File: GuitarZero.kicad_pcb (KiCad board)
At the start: 6 copper layers, 144 parts, among them J1 USB_A, J2 USB_B_Micro, J3 AudioJack3_SwitchT, J4 MCU_Debug, J6 Micro_SD_Card_Det_Hirose_DM3AT, SW1 SW_Push, SW2 SW_Push, SW3 SW_Push, SW4 SW_Push, SW5 SW_Push, SW6 SW_Push, U1 TPS54325, U10 FPGA_GPIO_Extra, U11 5x7 LED_matrix, U12 MCU_GPIO_Extra, U13 5x7 LED_matrix, U14 Power_Jumpers, U2 TSP54294, U3 XC7A100T-FTG256, U4 EFM32GG332, U5 S25FL127S, U6 Oscillator, U7 FPGA_JTAG_Debug, U8 PCM1754, U9 TPD_Current_Switch, Y1 Crystal_GND23

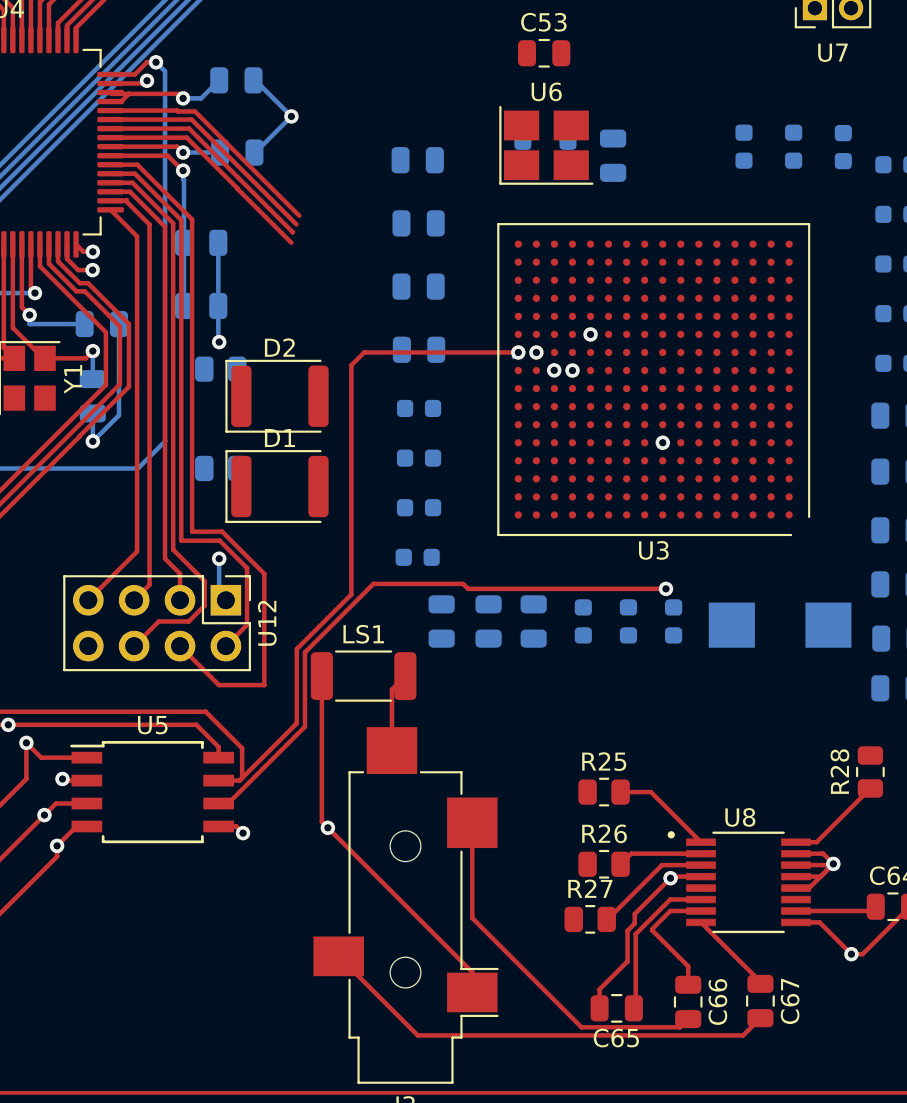
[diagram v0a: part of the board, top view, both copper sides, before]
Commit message: PCB: Grounded FPGA, wired MCU <-> FPGA
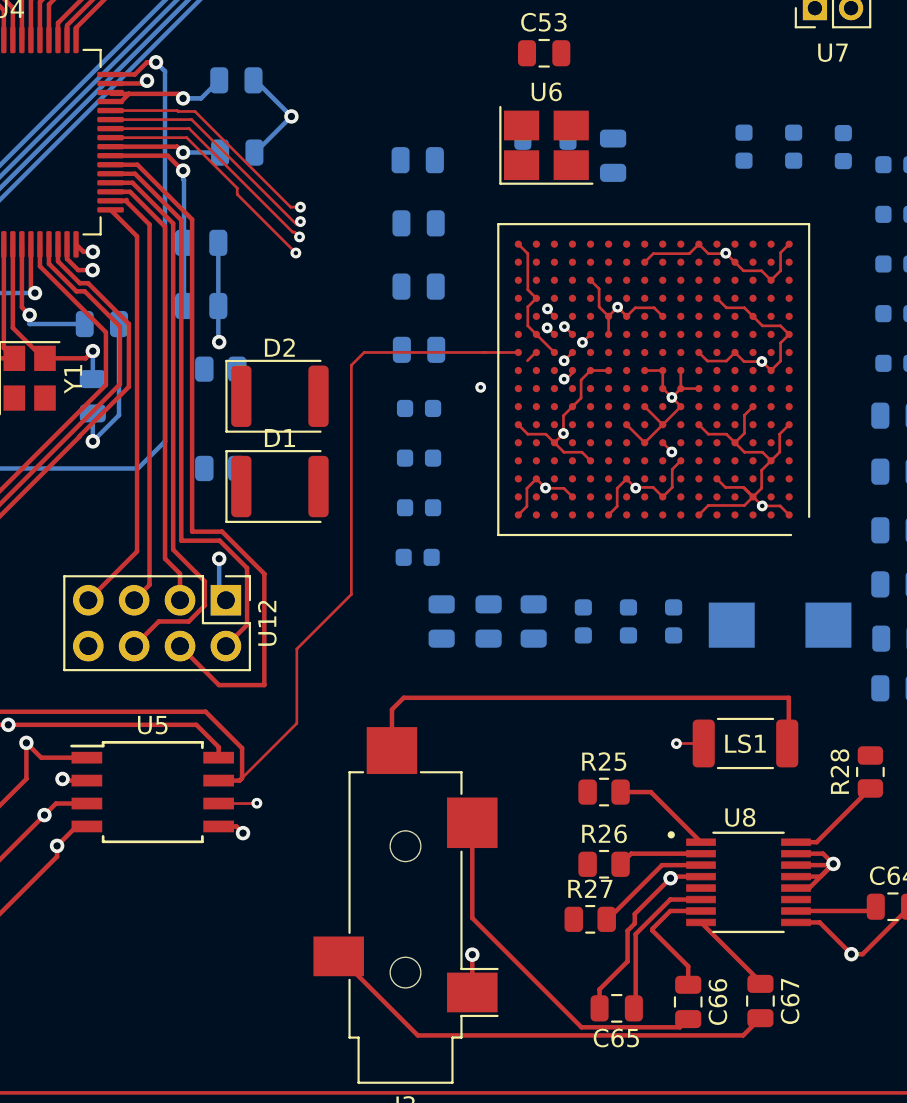
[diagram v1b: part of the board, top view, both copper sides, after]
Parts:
- moved LS1 21.5 mm to (202.8, 123.3)
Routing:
- net GND: track 327.6 -> 403.0 mm, vias 54 -> 63
- net Net-(J3-PadTN): track 4.43 -> 27.1 mm
- net /FPGA/MCU_SPI_MISO: track 12.9 -> 31.5 mm, vias 0 -> 2
- net /FPGA/MCU_SPI_Select: track 12.4 -> 31.0 mm, vias 0 -> 2
- net /FPGA/MCU_SPI_CLCK: track 12.5 -> 29.7 mm, vias 0 -> 2
- net /FPGA/MCU_SPI_MOSI: track 12.7 -> 29.5 mm, vias 0 -> 2
- net Net-(U3C-CCLK_0): track 41.4 -> 40.0 mm
- net Net-(U3A-IO_L2N_T0_D03_14): track 56.6 -> 56.3 mm, vias 1 -> 0
- net Net-(U3A-IO_L2P_T0_D02_14): track 53.4 -> 53.2 mm, vias 2 -> 1

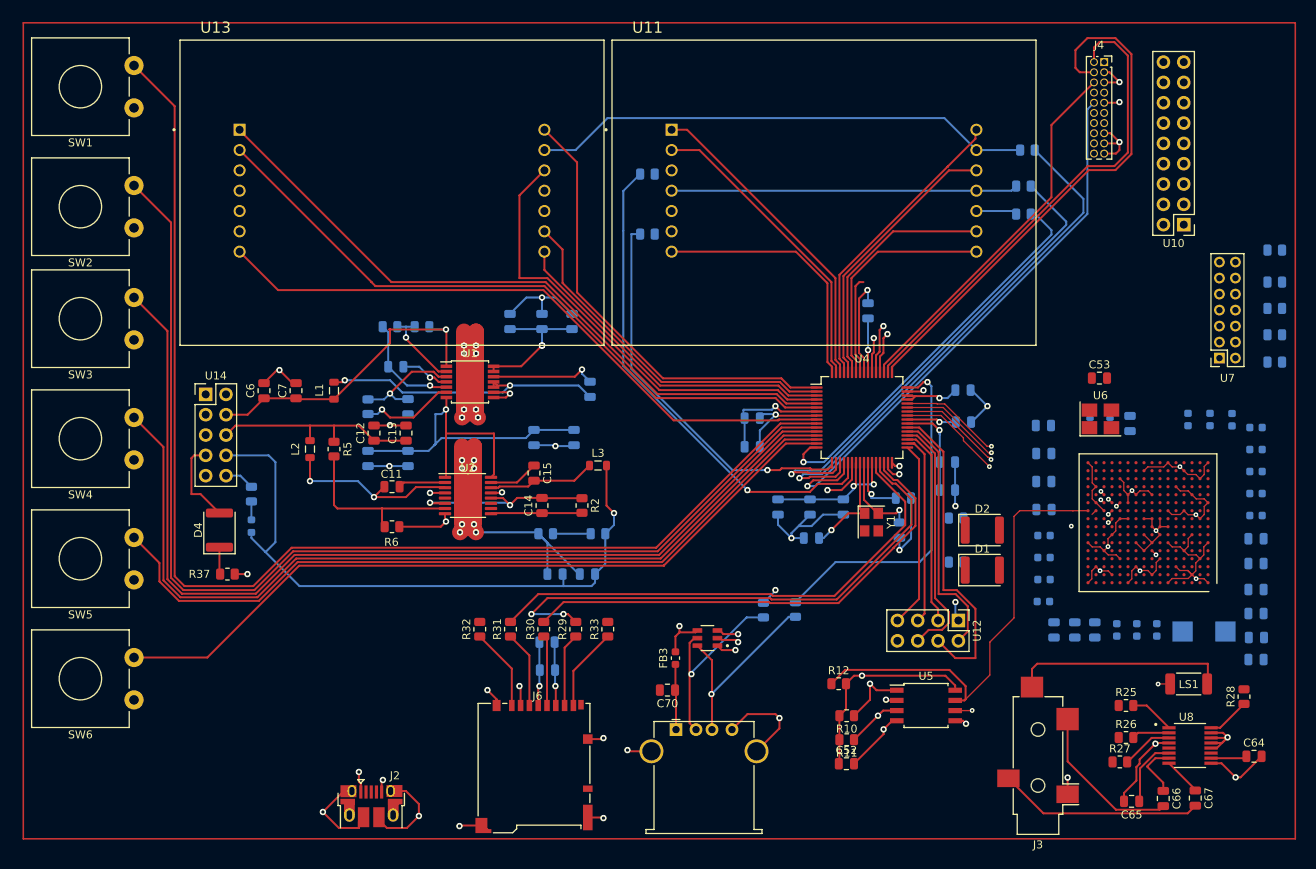
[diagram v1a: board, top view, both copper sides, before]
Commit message: Finished wiring for most of the FPGA
GPIO-extra pins remaining
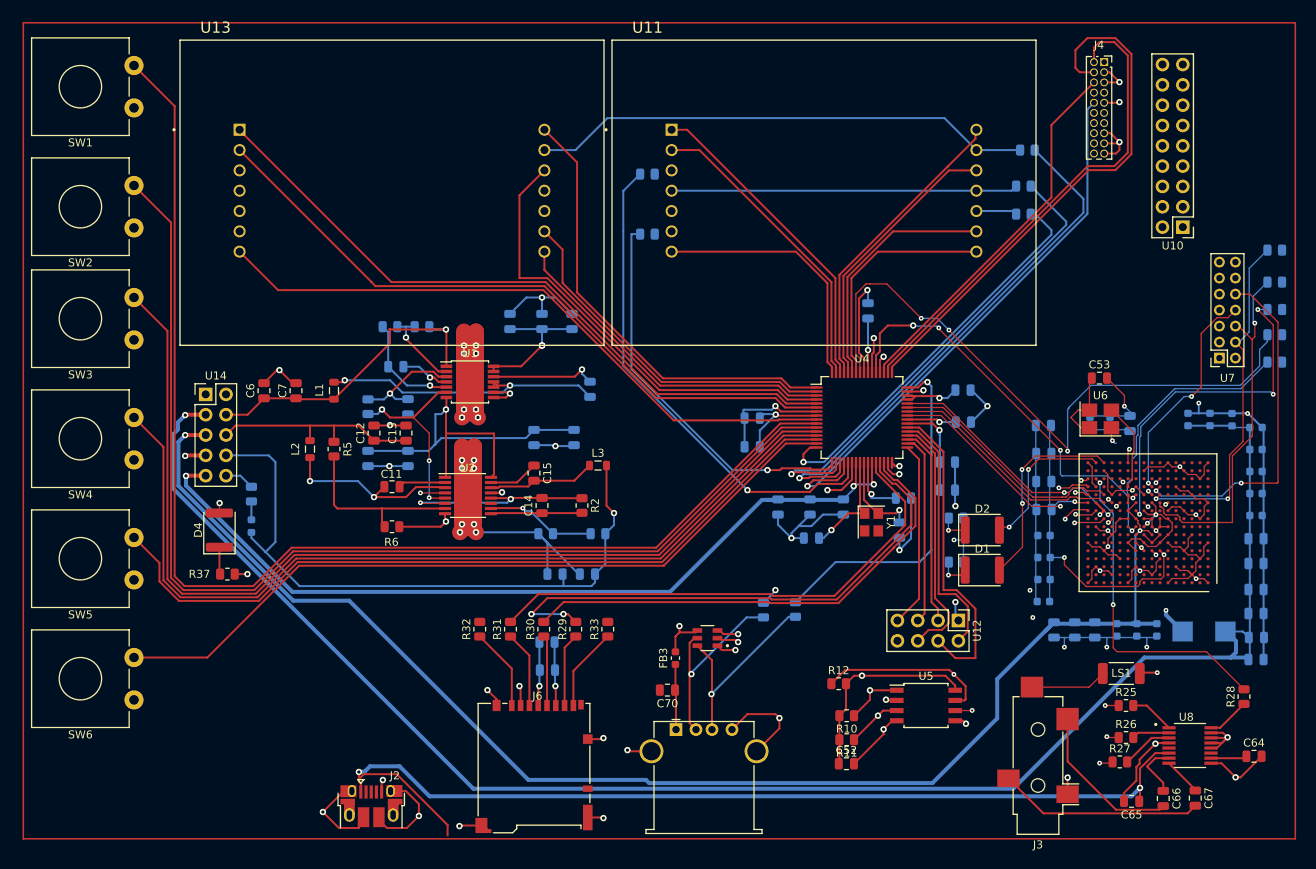
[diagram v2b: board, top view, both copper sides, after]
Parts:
- moved LS1 8.52 mm to (194.4, 122.0), turned to 180 degrees
- moved U10 0.33 mm to (202.1, 66.2)
- moved R15 0.14 mm to (213.6, 76.5)
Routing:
- net +1V0: track 0.00 -> 236.7 mm, vias 0 -> 3
- net +1V8: track 0.00 -> 192.1 mm, vias 0 -> 2
- net GND: track 403.0 -> 503.3 mm, vias 63 -> 77
- net +3.3VA: track 18.8 -> 116.3 mm, vias 2 -> 3
- net +5V: track 210.3 -> 304.1 mm, vias 5 -> 6
- net /FPGA/program_b: track 12.2 -> 95.8 mm, vias 0 -> 4
- net /FPGA/Done: track 6.15 -> 81.3 mm, vias 1 -> 4
- net +3.3V: track 93.5 -> 157.0 mm, vias 7 -> 16
- net Net-(U3C-TCK_0): track 0.00 -> 45.6 mm, vias 0 -> 1
- net /DAC/LEFT_RIGHT_CLOCK: track 0.00 -> 44.3 mm, vias 0 -> 2
- net Net-(U3C-TMS_0): track 0.00 -> 43.9 mm, vias 0 -> 2
- net Net-(U3C-TDI_0): track 0.00 -> 43.7 mm, vias 0 -> 2
- net Net-(U3C-INIT_B_0): track 0.00 -> 42.8 mm, vias 0 -> 3
- net /DAC/SYSTEM_CLOCK_INPUT: track 0.00 -> 40.5 mm, vias 0 -> 2
- net /DAC/DATA_INN: track 0.00 -> 40.4 mm, vias 0 -> 2
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
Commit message: Fixed 112 design error
FPGA GPIO pin headers still unrouted
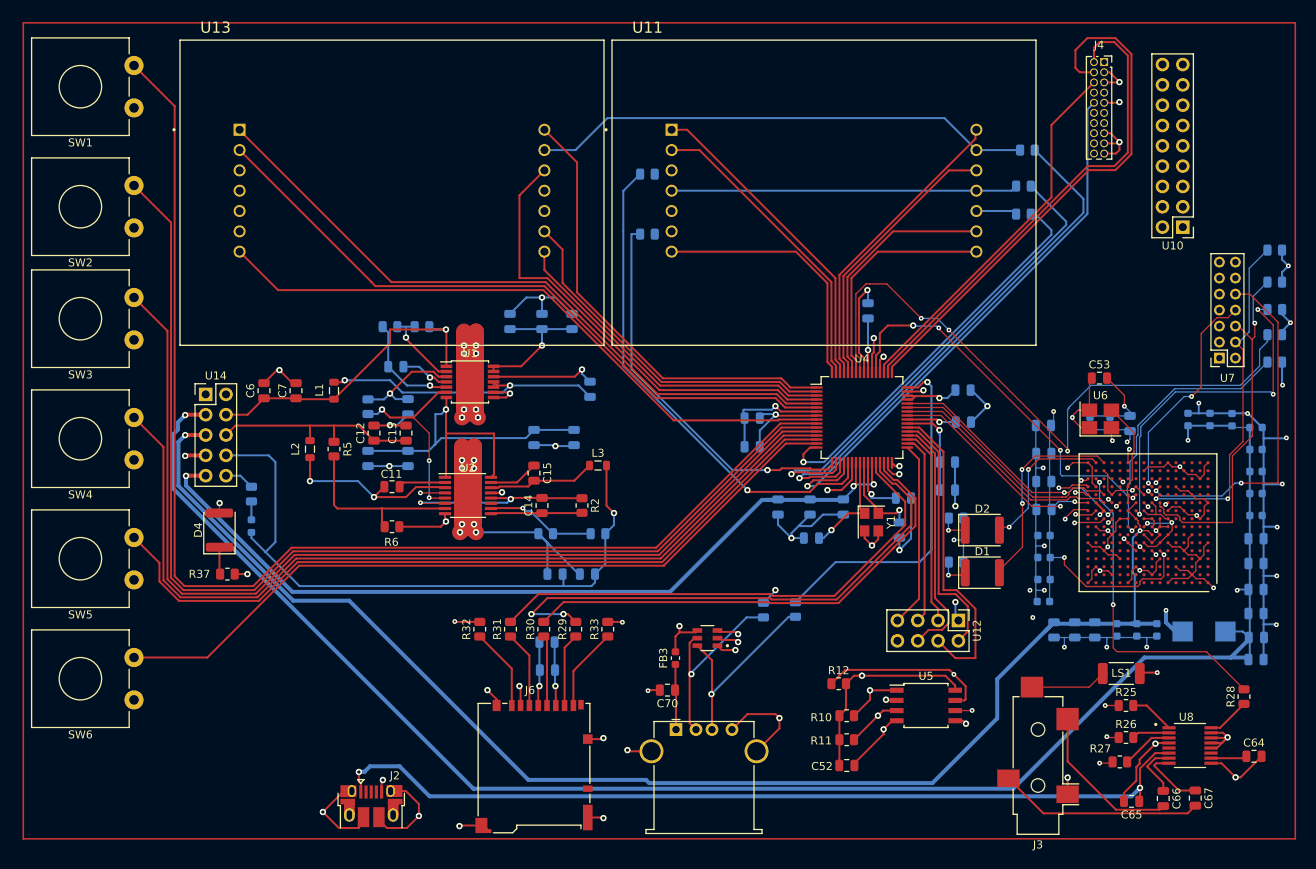
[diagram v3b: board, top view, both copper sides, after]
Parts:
- moved D1 0.33 mm to (177.0, 109.4)
- moved C52 0.23 mm to (160.1, 133.5)
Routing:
- net +1V0: track 236.7 -> 275.3 mm, vias 3 -> 7
- net GND: track 503.3 -> 529.2 mm, vias 77 -> 88
- net +3.3V: track 157.0 -> 174.2 mm, vias 16 -> 23
- net +5V: track 304.1 -> 289.5 mm, vias 6 -> 5
- net Net-(U8-VoutR): track 4.77 -> 8.44 mm
- net Net-(J6-DAT3/CD): track 66.2 -> 63.4 mm

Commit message: Moved board cutout to correct layer
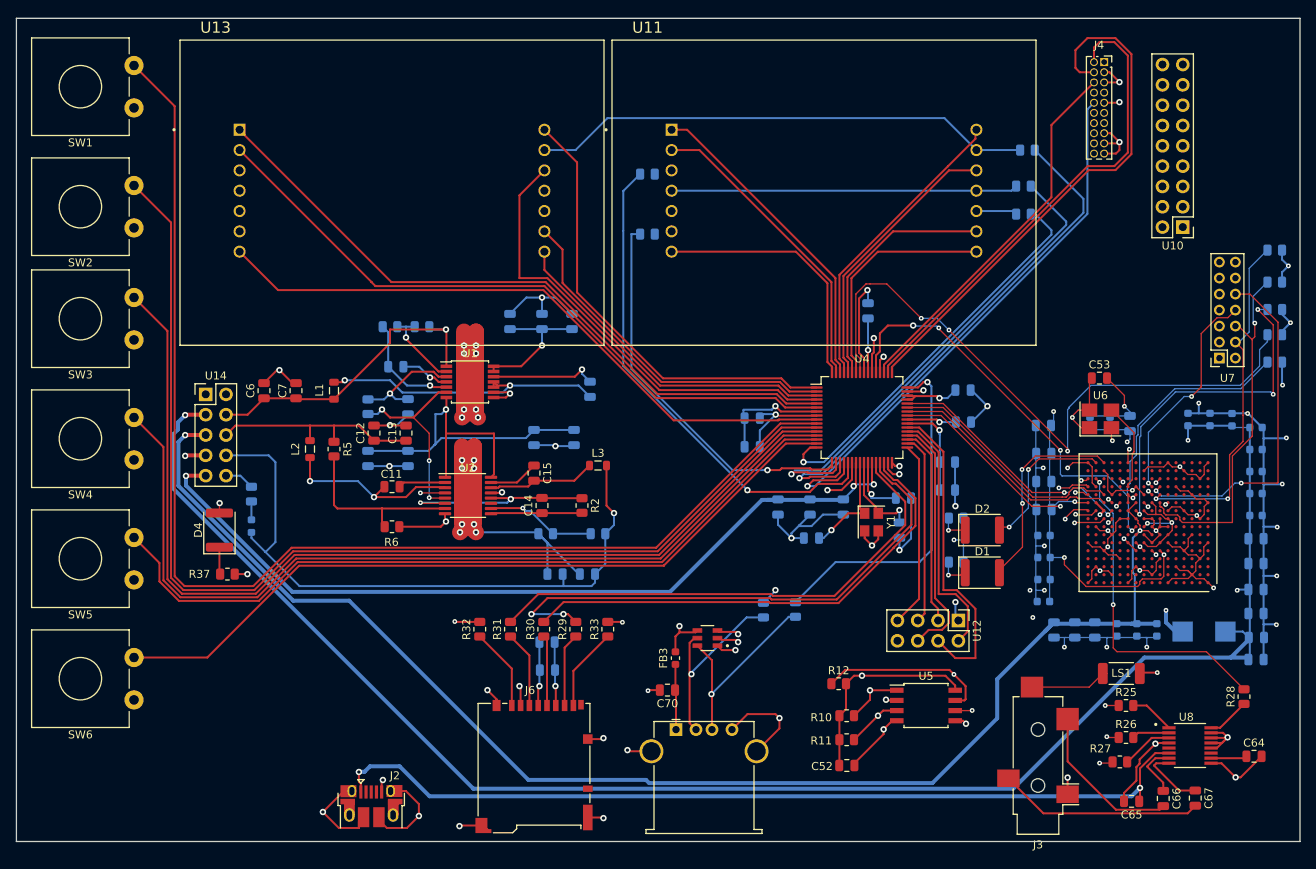
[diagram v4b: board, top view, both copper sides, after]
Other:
- board outline added: 160.4 x 102.9 mm
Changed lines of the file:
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@@
     )
   )
-  (gr_rect (start 57.161134 40.662942) (end 216.161134 142.662942)
-    (stroke (width 0.2) (type default)) (fill none) (layer "F.Cu"))
+  (gr_rect (start 56.3 40.1) (end 216.75 143)
+    (stroke (width 0.1) (type default)) (fill none) (layer "Edge.Cuts"))
   (segment (start 110.05 87.5) (end 110.05 88.95) (width 0.25) (layer "F.Cu") (net 1))
   (segment (start 196.75 136.3) (end 196.75 137.88) (width 0.25) (layer "F.Cu") (net 1))

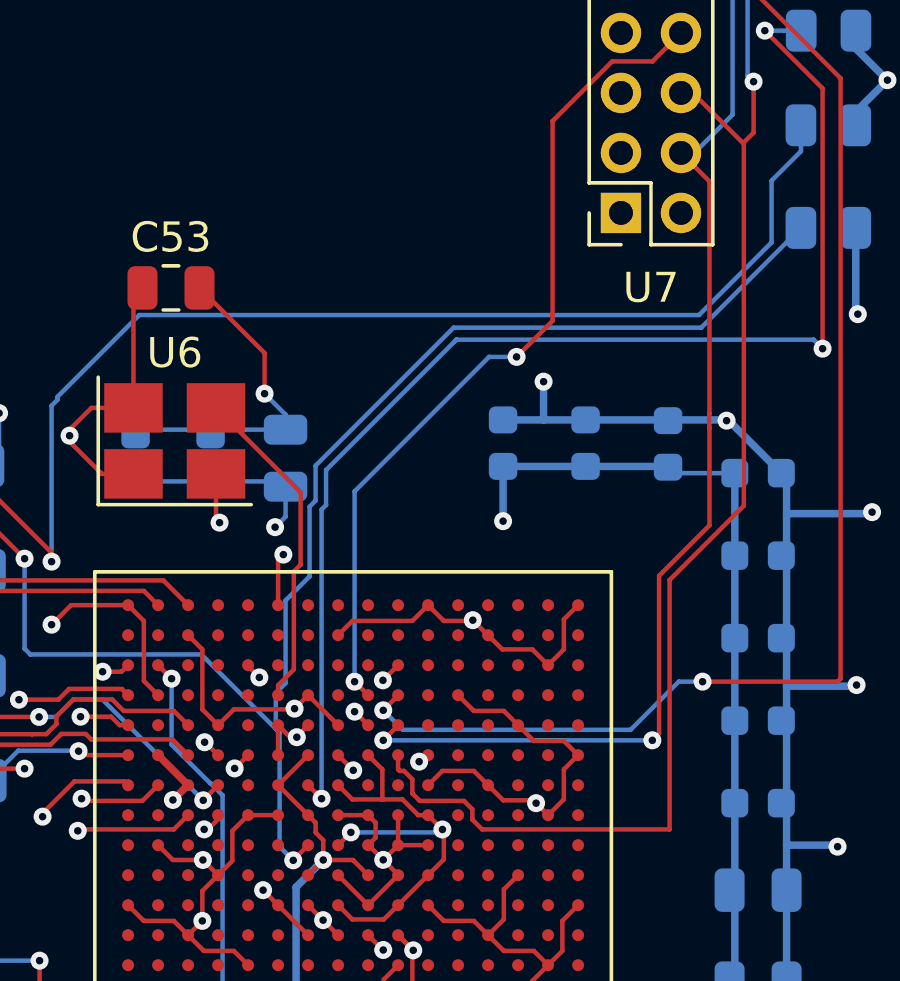
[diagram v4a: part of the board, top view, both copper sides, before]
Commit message: Grouped wires out from fpga to fpga pin header
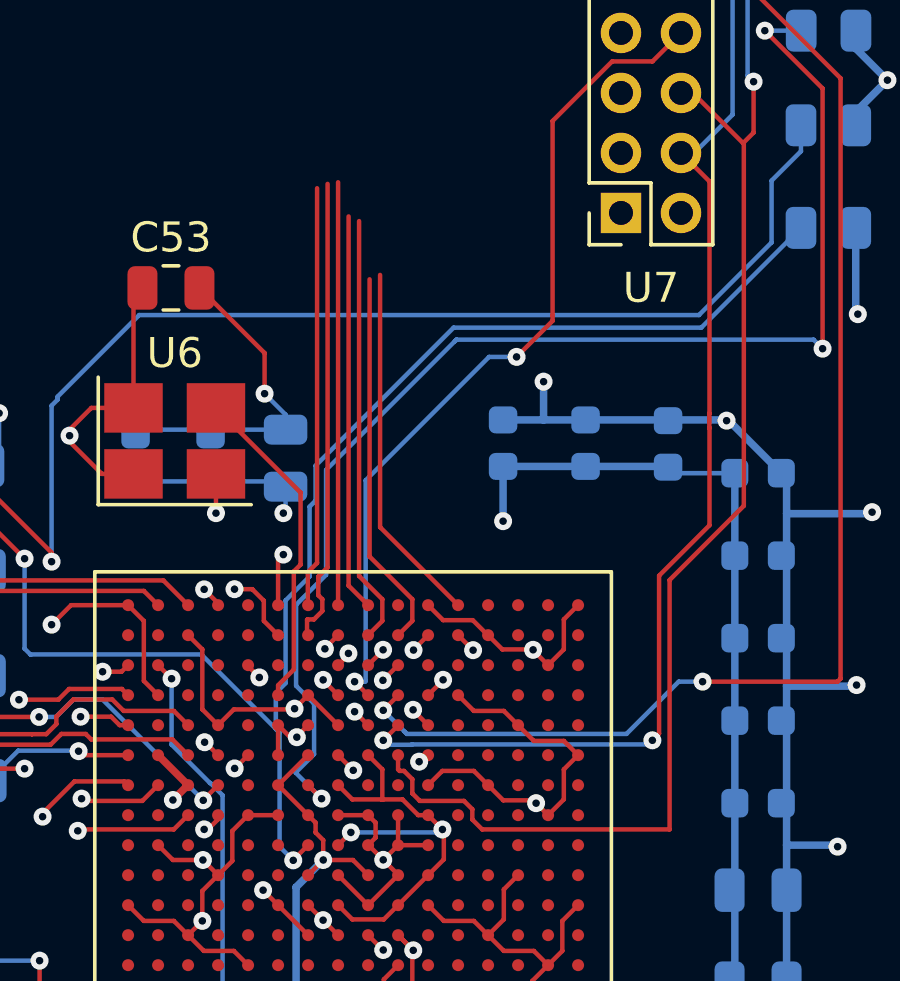
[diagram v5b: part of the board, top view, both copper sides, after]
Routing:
- net Net-(U10-GPIO_9): track 0.00 -> 19.4 mm, vias 0 -> 1
- net Net-(U10-GPIO_11): track 0.00 -> 17.9 mm, vias 0 -> 1
- net Net-(U10-GPIO_7): track 0.00 -> 17.2 mm, vias 0 -> 1
- net Net-(U10-GPIO_5): track 0.00 -> 15.7 mm, vias 0 -> 1
- net Net-(U10-GPIO_13): track 0.00 -> 15.6 mm
- net Net-(U10-GPIO_3): track 0.00 -> 14.5 mm, vias 0 -> 1
- net Net-(U10-GPIO_2): track 0.00 -> 14.3 mm
- net Net-(U10-GPIO_6): track 0.00 -> 14.1 mm
- net Net-(U10-GPIO_8): track 0.00 -> 14.0 mm
- net Net-(U10-GPIO_10): track 0.00 -> 13.7 mm, vias 0 -> 1
- net Net-(U10-GPIO_15): track 0.00 -> 13.3 mm, vias 0 -> 1
- net Net-(U10-GPIO_4): track 0.00 -> 13.2 mm
- net Net-(U10-GPIO_14): track 0.00 -> 13.0 mm, vias 0 -> 1
- net Net-(U10-GPIO_1): track 0.00 -> 13.0 mm, vias 0 -> 1
- net Net-(U10-GPIO_16): track 0.00 -> 12.7 mm
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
